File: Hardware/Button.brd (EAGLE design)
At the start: 50 x 91.8 mm, 39 parts, among them IC1 STM32F030C6T, IC2 MCP73831, M2 WIRELESS-NRF24L01, Q1 IRLML5203, Q2 BC817-16LT1SMD, Q3 BC817-16LT1SMD, X1 MINI-USB-UX60-MB-5ST

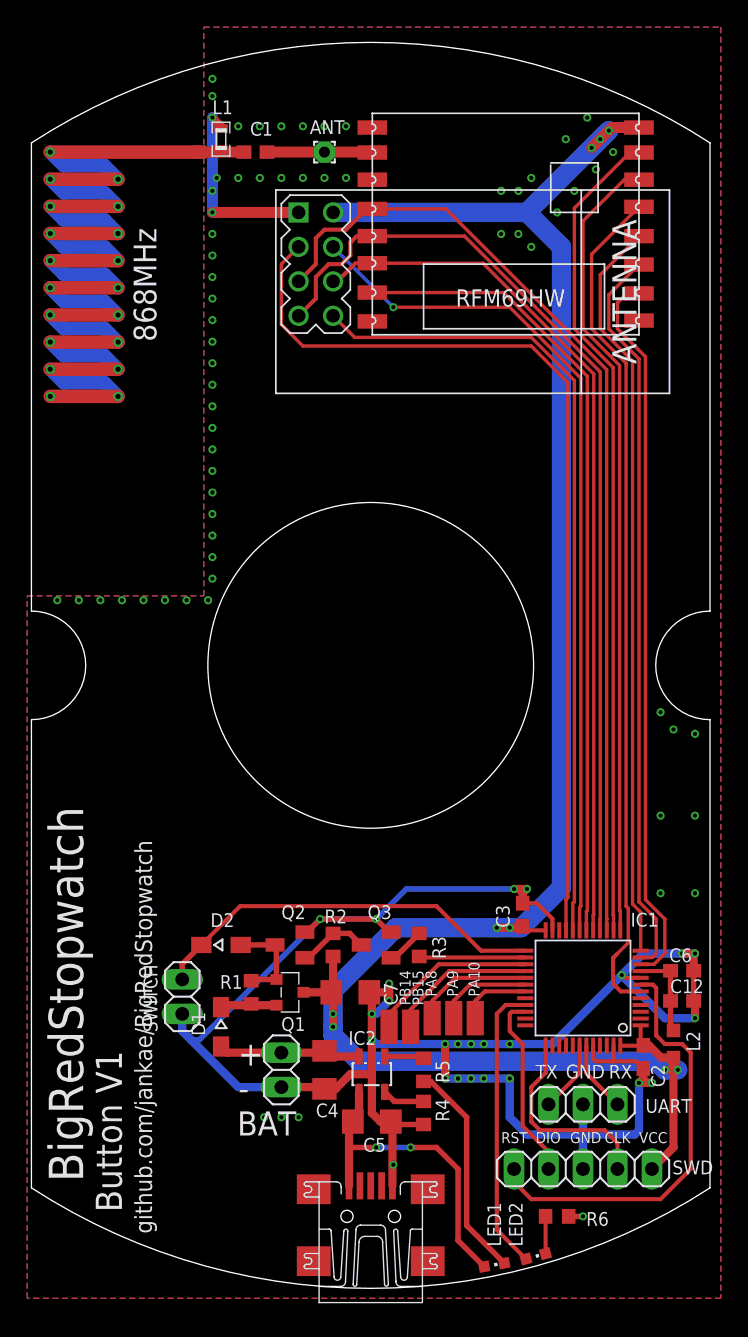
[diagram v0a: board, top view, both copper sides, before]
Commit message: LED output added to button
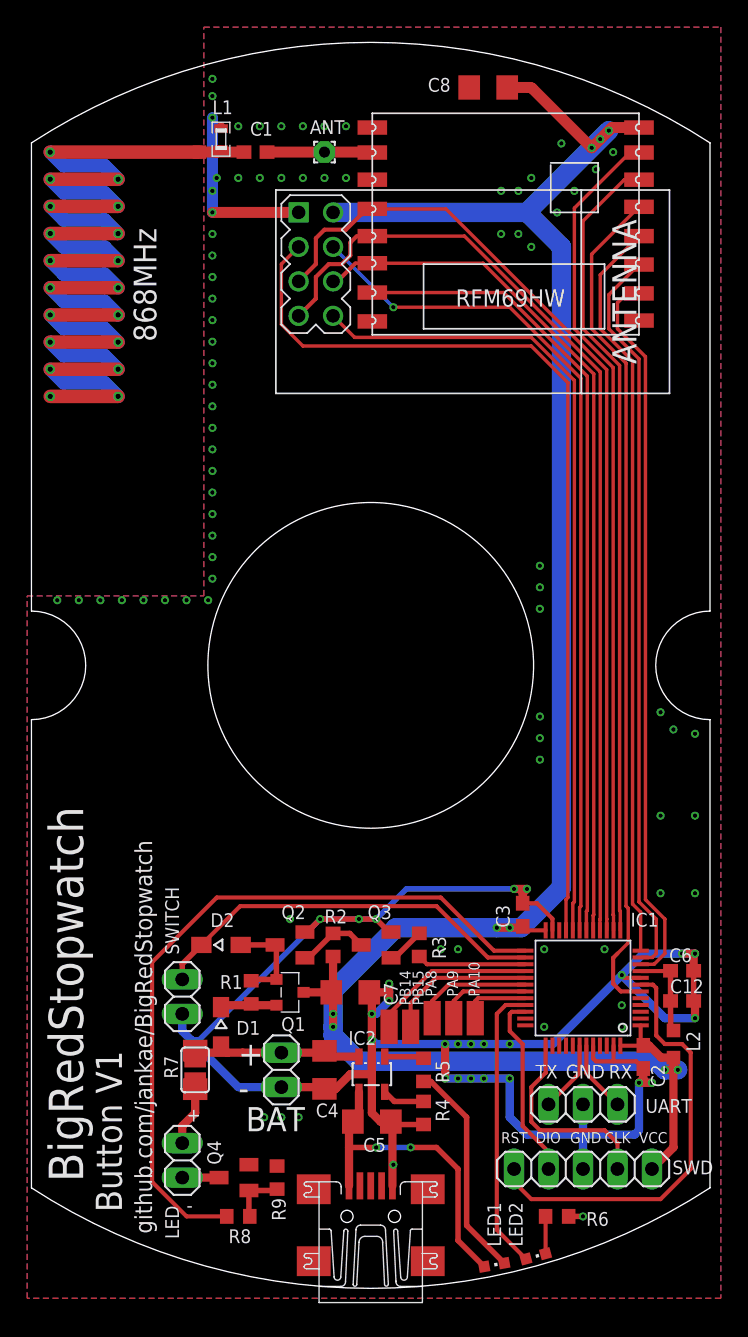
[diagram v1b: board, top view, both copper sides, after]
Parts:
- added C8: 10u/10V, rcl:C1206
- added LED: (no value), pinhead:1X02
- added Q4: BSS123, transistor-small-signal:SOT23
- added R7: n.p., rcl:R1206
- added R8: 1k, rcl:R0603
- added R9: 100k, rcl:R0603
- added SJ1: (no value), jumper:SJ
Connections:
- new net N$13: LED.1, Q4.3
- new net N$17: LED.2, R7.1, SJ1.1
- new net N$18: Q4.1, R8.1, R9.1
- new net N$19: IC1.25, R8.2
- net DISABLE: now also IC1.27; no longer IC1.26
- net GND: now also C8.1, Q4.2, R9.2
- net N$11: now also IC1.29; no longer IC1.28
- net N$12: now also IC1.28; no longer IC1.27
- net N$14: now also IC1.32; no longer IC1.31
- net N$15: now also IC1.31; no longer IC1.30
- net N$16: now also IC1.30; no longer IC1.29
- net SWITCH: now also IC1.26; no longer IC1.25
- net V+: now also R7.2, SJ1.2
- net VCC: now also C8.2
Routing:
- net N$19: track 0.00 -> 53.8 mm
- net VCC: track 156.3 -> 164.4 mm
- net N$17: track 0.00 -> 4.37 mm
- net N$18: track 0.00 -> 4.05 mm
- net N$13: track 0.00 -> 2.71 mm
- net V+: track 10.6 -> 13.0 mm
- net GND: track 177.0 -> 176.1 mm, vias 91 -> 105

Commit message: Second iteration of display board
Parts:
- moved X1 0.48 mm to (25.0, 4.92)
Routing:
- net V+: track 13.0 -> 13.7 mm
- net N$17: track 4.37 -> 5.03 mm
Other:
- board text added: "08/17"
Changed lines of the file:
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@@
 <setting verticaltext="up"/>
 </settings>
-<grid distance="0.0125" unitdist="inch" unit="inch" style="lines" multiple="1" display="yes" altdistance="0.00625" altunitdist="inch" altunit="inch"/>
+<grid distance="0.0125" unitdist="inch" unit="mm" style="lines" multiple="1" display="yes" altdistance="0.00625" altunitdist="inch" altunit="inch"/>
 <layers>
 <layer number="1" name="Top" color="4" fill="1" visible="yes" active="yes"/>
@@
 <layer number="23" name="tOrigins" color="15" fill="1" visible="yes" active="yes"/>
 <layer number="24" name="bOrigins" color="15" fill="1" visible="yes" active="yes"/>
-<layer number="25" name="tNames" color="7" fill="1" visible="yes" active="yes"/>
+<layer number="25" name="tNames" color="7" fill="1" visible="no" active="yes"/>
 <layer number="26" name="bNames" color="7" fill="1" visible="no" active="yes"/>
 <layer number="27" name="tValues" color="7" fill="1" visible="no" active="yes"/>
@@
 <text x="11.43" y="12.3825" size="1.016" layer="21" font="vector">+</text>
 <text x="11.43" y="5.715" size="1.016" layer="21" font="vector">-</text>
+<text x="6.6675" y="31.4325" size="1.9304" layer="21" font="vector" rot="R90">08/17</text>
 </plain>
 <attributes>
@@
 <attribute name="VALUE" x="38.1" y="26.9875" size="1.27" layer="27" rot="R90"/>
 </element>
-<element name="X1" library="con-hirose" package="UX60-MB-5ST" value="MINI-USB-UX60-MB-5ST" x="25" y="5.3975" smashed="yes" rot="R90">
-<attribute name="MPN" value="" x="25" y="5.3975" size="1.778" layer="27" font="vector" rot="R90" display="off"/>
-<attribute name="MF" value="" x="25" y="5.3975" size="1.778" layer="27" font="vector" rot="R90" display="off"/>
-<attribute name="OC_FARNELL" value="unknown" x="25" y="5.3975" size="1.778" layer="27" font="vector" rot="R90" display="off"/>
-<attribute name="OC_NEWARK" value="unknown" x="25" y="5.3975" size="1.778" layer="27" font="vector" rot="R90" display="off"/>
-<attribute name="VALUE" x="31.985" y="0.9525" size="1.27" layer="27" rot="R90"/>
+<element name="X1" library="con-hirose" package="UX60-MB-5ST" value="MINI-USB-UX60-MB-5ST" x="25" y="4.92125" smashed="yes" rot="R90">
+<attribute name="MPN" value="" x="25" y="4.92125" size="1.778" layer="27" font="vector" rot="R90" display="off"/>
+<attribute name="MF" value="" x="25" y="4.92125" size="1.778" layer="27" font="vector" rot="R90" display="off"/>
+<attribute name="OC_FARNELL" value="unknown" x="25" y="4.92125" size="1.778" layer="27" font="vector" rot="R90" display="off"/>
+<attribute name="OC_NEWARK" value="unknown" x="25" y="4.92125" size="1.778" layer="27" font="vector" rot="R90" display="off"/>
+<attribute name="VALUE" x="31.985" y="0.47625" size="1.27" layer="27" rot="R90"/>
 </element>
 <element name="IC2" library="mcp" package="SOT23-5" value="MCP73831" x="25.0825" y="15.875" smashed="yes" rot="R180">
@@
 <contactref element="X1" pad="5"/>
 <contactref element="BAT" pad="1"/>
-<wire x1="26.6" y1="7.6475" x2="26.6" y2="12.265" width="0.6096" layer="1"/>
+<wire x1="26.6" y1="7.17125" x2="26.6" y2="12.265" width="0.6096" layer="1"/>
 <wire x1="26.6" y1="12.265" x2="26.4825" y2="12.3825" width="0.6096" layer="1"/>
 <wire x1="25.0825" y1="17.175" x2="25.0825" y2="15.875" width="0.6096" layer="1"/>
@@
 <vertex x="50.8" y="-0.635"/>
 <vertex x="-0.3175" y="-0.635"/>
-<vertex x="-0.3175" y="51.1175"/>
+<vertex x="-0.3175" y="38.1"/>
 <vertex x="12.7" y="51.1175"/>
 </polygon>
@@
 <vertex x="50.8" y="-0.635"/>
 <vertex x="-0.3175" y="-0.635"/>
-<vertex x="-0.3175" y="51.1175"/>
+<vertex x="-0.3175" y="38.1"/>
 <vertex x="12.7" y="51.1175"/>
 </polygon>
@@
 <via x="13.335" y="52.3875" extent="1-16" drill="0.3048" shape="octagon"/>
 <via x="13.0175" y="50.8" extent="1-16" drill="0.3048" shape="octagon"/>
-<via x="11.43" y="50.8" extent="1-16" drill="0.3048" shape="octagon"/>
-<via x="9.8425" y="50.8" extent="1-16" drill="0.3048" shape="octagon"/>
-<via x="8.255" y="50.8" extent="1-16" drill="0.3048" shape="octagon"/>
-<via x="6.6675" y="50.8" extent="1-16" drill="0.3048" shape="octagon"/>
-<via x="5.08" y="50.8" extent="1-16" drill="0.3048" shape="octagon"/>
-<via x="3.4925" y="50.8" extent="1-16" drill="0.3048" shape="octagon"/>
-<via x="1.905" y="50.8" extent="1-16" drill="0.3048" shape="octagon"/>
+<via x="11.43" y="49.2125" extent="1-16" drill="0.3048" shape="octagon"/>
+<via x="9.8425" y="47.625" extent="1-16" drill="0.3048" shape="octagon"/>
+<via x="8.255" y="46.0375" extent="1-16" drill="0.3048" shape="octagon"/>
+<via x="6.6675" y="44.45" extent="1-16" drill="0.3048" shape="octagon"/>
+<via x="5.08" y="42.8625" extent="1-16" drill="0.3048" shape="octagon"/>
+<via x="3.4925" y="41.275" extent="1-16" drill="0.3048" shape="octagon"/>
+<via x="1.905" y="39.6875" extent="1-16" drill="0.3048" shape="octagon"/>
 <via x="21.59" y="85.725" extent="1-16" drill="0.3048" shape="octagon"/>
 <via x="23.1775" y="85.725" extent="1-16" drill="0.3048" shape="octagon"/>
@@
 <wire x1="21.59" y1="17.5925" x2="21.46" y2="17.4625" width="0.6096" layer="1"/>
 <wire x1="21.46" y1="17.4625" x2="18.415" y2="17.4625" width="0.6096" layer="1"/>
-<wire x1="18.415" y1="17.4625" x2="15.5575" y2="17.4625" width="0.6096" layer="1"/>
-<wire x1="15.5575" y1="17.4625" x2="14.425" y2="17.4625" width="0.6096" layer="1"/>
+<wire x1="18.415" y1="17.4625" x2="14.425" y2="17.4625" width="0.6096" layer="1"/>
 <wire x1="14.425" y1="17.4625" x2="13.97" y2="17.9175" width="0.6096" layer="1"/>
 <contactref element="R7" pad="2"/>
@@
 <wire x1="12.065" y1="17.6145" x2="12.217" y2="17.4625" width="0.6096" layer="1"/>
 <wire x1="12.217" y1="17.4625" x2="14.425" y2="17.4625" width="0.6096" layer="1"/>
-<wire x1="12.217" y1="17.4625" x2="12.065" y2="16.9545" width="0" layer="19" extent="1-1"/>
+<wire x1="12.065" y1="16.9545" x2="12.065" y2="17.6145" width="0.8128" layer="1"/>
 </signal>
 <signal name="SWITCH">
@@
 <contactref element="C5" pad="1"/>
 <contactref element="LED1" pad="A"/>
-<wire x1="23.4" y1="7.6475" x2="23.4" y2="10.4775" width="0.6096" layer="1"/>
+<wire x1="23.4" y1="7.17125" x2="23.4" y2="10.4775" width="0.6096" layer="1"/>
 <wire x1="23.4" y1="10.4775" x2="23.4" y2="12.1" width="0.6096" layer="1"/>
 <wire x1="23.4" y1="12.1" x2="23.6825" y2="12.3825" width="0.6096" layer="1"/>
@@
 <wire x1="36.39" y1="22.975" x2="29.80125" y2="22.975" width="0.3048" layer="1"/>
 <wire x1="29.80125" y1="22.975" x2="27.94" y2="21.11375" width="0.3048" layer="1"/>
-<wire x1="27.94" y1="19.05" x2="27.94" y2="19.3675" width="0" layer="19" extent="1-1"/>
+<wire x1="27.94" y1="19.3675" x2="27.94" y2="19.05" width="0.8128" layer="1"/>
 </signal>
 <signal name="N$12">
@@
 <wire x1="11.1125" y1="12.065" x2="12.065" y2="13.0175" width="0.6096" layer="1"/>
 <wire x1="12.065" y1="13.0175" x2="12.065" y2="14.7705" width="0.6096" layer="1"/>
-<wire x1="12.065" y1="14.7705" x2="12.065" y2="15.4305" width="0" layer="19" extent="1-1"/>
+<wire x1="12.065" y1="14.7705" x2="12.065" y2="15.4305" width="0.8128" layer="1"/>
 </signal>
 <signal name="N$18">

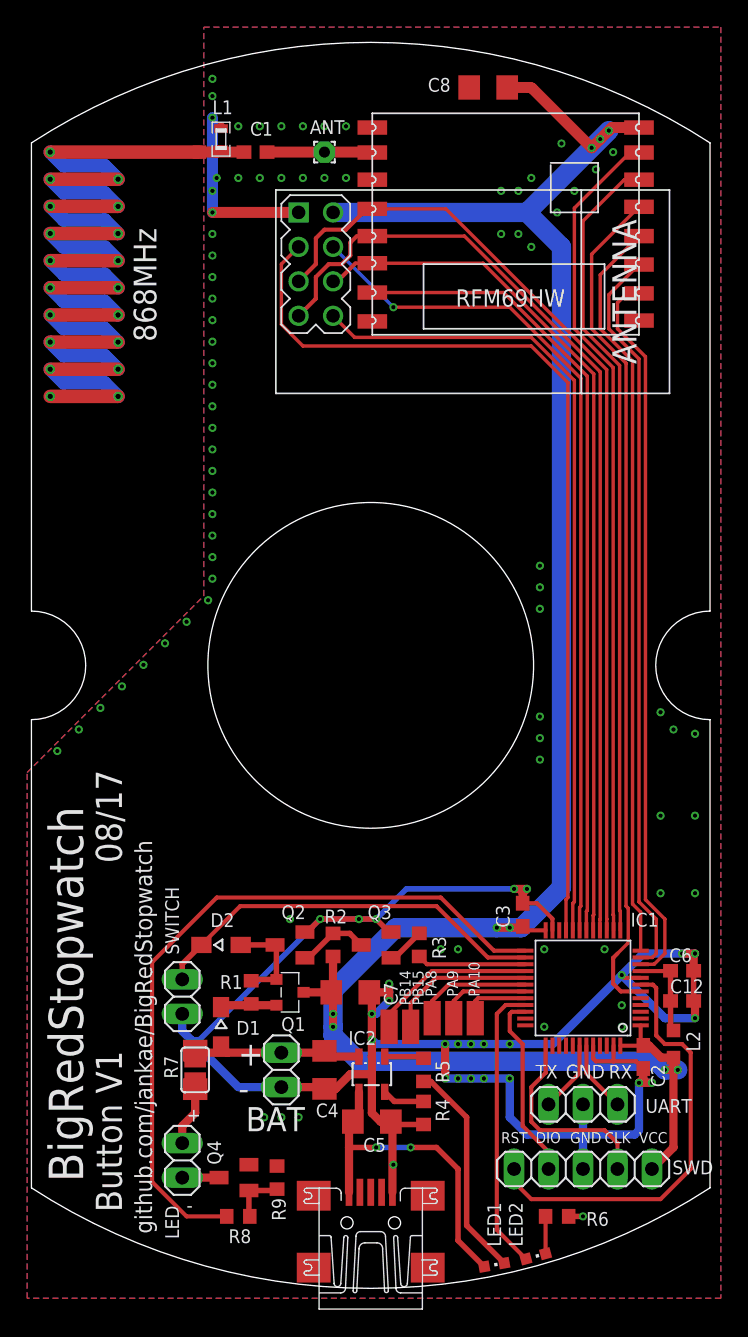
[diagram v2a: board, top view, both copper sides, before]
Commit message: 3V LDO + voltage sensing
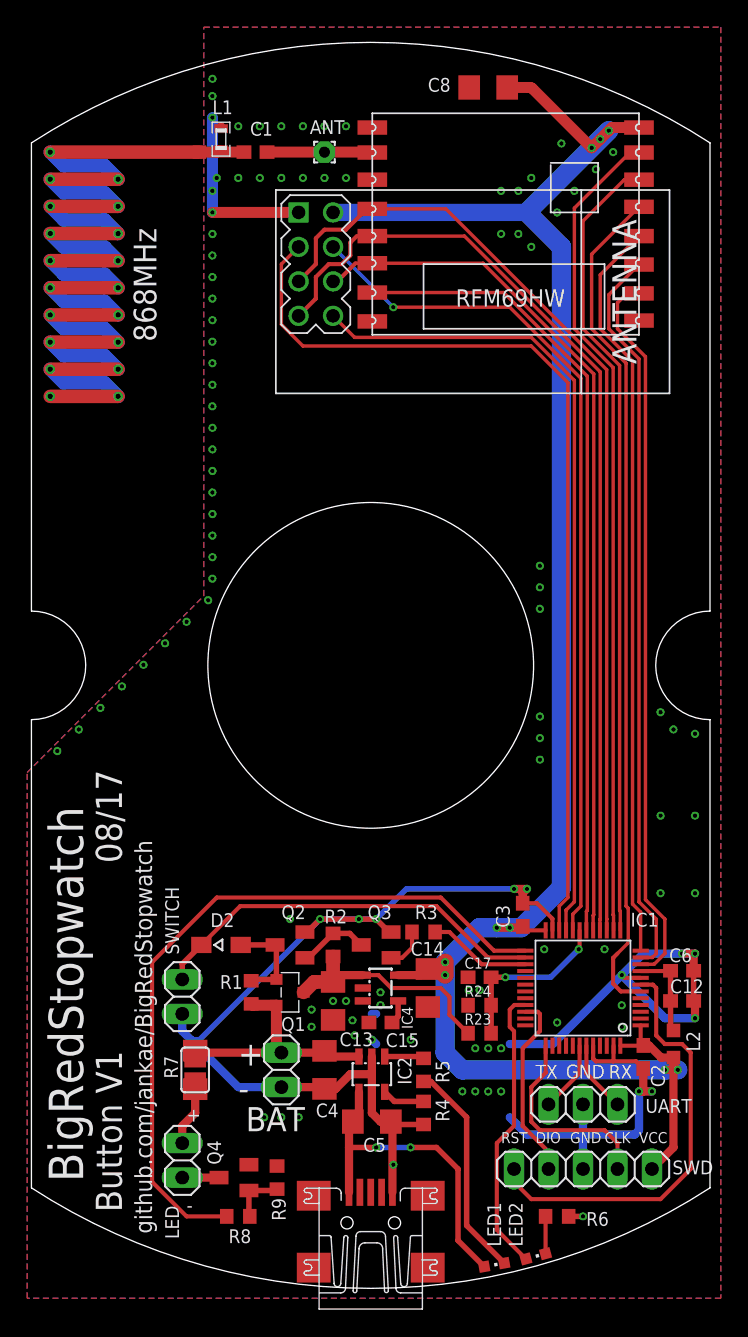
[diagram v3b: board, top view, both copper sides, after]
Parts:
- removed C7: 10u/10V, rcl:C1206
- removed D1: 1N4148, diode:SOD323-W
- removed PA10, PA8, PA9, PB14, PB15: (no value), wirepad:SMD1,27-2,54
- added C13, C14: 10u/10V, rcl:C1206
- added C15: 10n, rcl:C0603
- added C17: 100n, rcl:C0603
- added IC4: LP2985M5, v-reg-3:SOT23-5
- added R23, R24: 100k, rcl:R0603
- moved R3 1.00 mm to (28.9, 26.4), turned to 0 degrees
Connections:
- removed net N$11: IC1.29, PB15.1
- removed net N$12: IC1.28, PB14.1
- removed net N$14: IC1.32, PA10.1
- removed net N$15: IC1.31, PA9.1
- removed net N$16: IC1.30, PA8.1
- removed net N$6: D1.C, Q1.2, R1.1
- new net N$30: C15.2, IC4.4
- new net N$31: C17.1, IC1.19, R23.2, R24.1
- new net VDD: C14.1, C2.1, C3.1, C8.2, IC1.1, IC1.24, IC1.48, IC4.5, L2.1, M2.2, SWD.1, U$1.VCC
- net CS_NRF24: now also IC1.20; no longer IC1.19
- net GND: now also C13.2, C14.2, C15.1, C17.2, IC4.2, IC4.3, R24.2; no longer C7.2
- net NRF24_CE: now also IC1.22; no longer IC1.21
- net NRF24_IRQ: now also IC1.21; no longer IC1.20
- net V+: now also Q1.2, R1.1; no longer D1.A
- net VCC: now also C13.1, IC4.1, R23.1; no longer C2.1, C3.1, C7.1, C8.2, IC1.1, IC1.24, IC1.48, L2.1, M2.2, SWD.1, U$1.VCC
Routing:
- net VDD: track 0.00 -> 147.8 mm, vias 0 -> 9
- net VCC: track 164.4 -> 17.1 mm, vias 9 -> 0
- net GND: track 176.6 -> 146.4 mm, vias 105 -> 108
- net N$31: track 0.00 -> 12.9 mm, vias 0 -> 2
- net N$12: track 12.3 -> 0.00 mm
- net N$11: track 11.7 -> 0.00 mm
- net N$16: track 8.63 -> 0.00 mm
- net N$15: track 6.84 -> 0.00 mm
- net N$14: track 5.04 -> 0.00 mm
- net V+: track 13.7 -> 18.7 mm
- net N$6: track 4.24 -> 0.00 mm
- net N$30: track 0.00 -> 1.78 mm
- net DISABLE: track 8.16 -> 7.63 mm
